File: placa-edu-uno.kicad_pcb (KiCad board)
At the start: 2 copper layers, 97.1 x 58.9 mm, 71 parts, among them J1 Conn_02x20_Odd_Even_MountingP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, J10 HEADER, J11 HEADER, J12 HEADER, J13 HEADER, J14 HEADER, J15 HEADER, J2 Screw_Terminal_01x02, J3 Screw_Terminal_01x02, J4 Screw_Terminal_01x02, J5 Screw_Terminal_01x02, J6 Conn_02x13_Odd_Even, J7 HEADER, J8 HEADER, J9 HEADER, U1 PCA9685, U2 MAX98357AETE_T, U3 MAX98357AETE_T, U4 ICS-43434, U5 ICS-43434, U6 LM73605

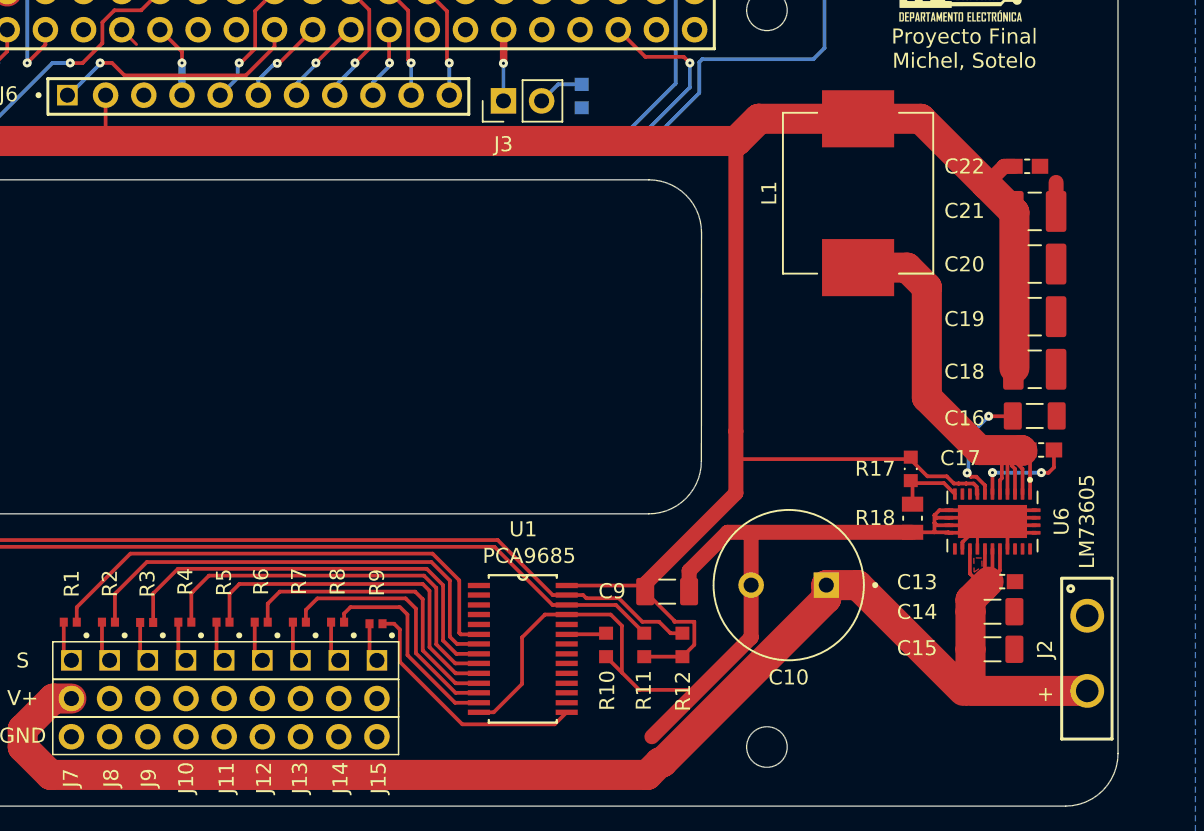
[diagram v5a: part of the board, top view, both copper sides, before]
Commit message: Se arranca un nuevo diseno. Se saco el regulador y 4 servos. Hay que reajustar el diseno del PCB.
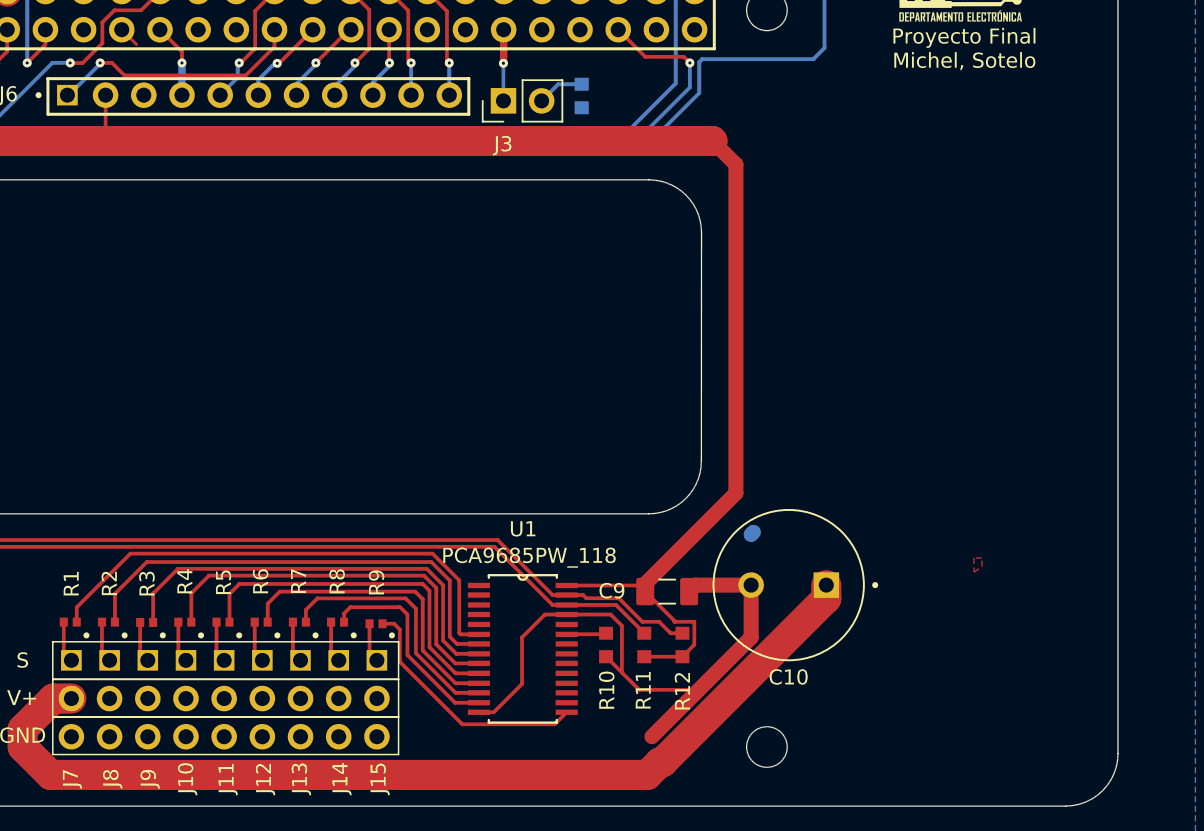
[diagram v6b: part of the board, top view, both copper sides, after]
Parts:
- removed C13, C22: 0.47 uF, CC0603KRX7R7BB474:CAPC1608X90
- removed C14, C15: 10 uF, CL31B106KOHNNNE:CAPC3216X180N
- removed C16: 2.2uF, CL31B225KOHNNNE:CAPC3216X180N
- removed C17: 0.47uF, CC0603KRX7R7BB474:CAPC1608X90
- removed C18, C19, C20, C21: 22uF, CL32B226KOJNNNE:CAPC3225X270N
- removed J2: Screw_Terminal_01x02, 691253700002:691253700002
- removed L1: 4.7uH, SPM10040T-4R7M:IND_SPM10040T-4R7M
- removed R17: 100k, 0603WAJ0104T5E:RESC1608X55N
- removed R18: 24.3k, 0805W8F2432T5E:RESC2012X65N
- removed U6: LM73605, LM73606RNPT-copia:QFN50P600X400X80-31N
- U1: value PCA9685 -> PCA9685PW_118
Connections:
- U1 pad 10: /Driver Servos/J4 -> unconnected-(U1-LED4-Pad10)
- U1 pad 11: /Driver Servos/J5 -> unconnected-(U1-LED5-Pad11)
- U1 pad 12: /Driver Servos/J6 -> unconnected-(U1-LED6-Pad12)
- U1 pad 13: /Driver Servos/J7 -> unconnected-(U1-LED7-Pad13)
- U1 pad 15: /Driver Servos/J8 -> unconnected-(U1-LED8-Pad15)
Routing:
- net 5V_RPI: track 190.1 -> 135.1 mm
- net GND: track 143.8 -> 89.8 mm
- net 5V_Fuente: track 103.1 -> 65.2 mm
- net Net-(C17-Pad1): track 34.3 -> 0.00 mm
- net Net-(U6-VCC): track 8.12 -> 0.00 mm, vias 2 -> 0
- net Net-(U6-CBOOT): track 7.07 -> 0.00 mm, vias 2 -> 0
- net Net-(U6-FB): track 4.69 -> 0.00 mm
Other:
- board text added: "FRENTE"

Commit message: Se borro todo y se arranco de nuevo. Placa circular.
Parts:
- removed J11, J12, J13, J14, J15: HEADER, TSW-101-07-T-T:SAMTEC_TSW-101-07-T-T
- removed the MountingHole at (3.50, 3.50)
- removed the MountingHole at (3.50, 52.5)
- removed R5, R6, R7, R8, R9: 220, RC0402FR-07220RL:RESC1005X40N
- U1: value PCA9685PW_118 -> PCA9685
- U2, U3: value MAX98357AETE_T -> MAX98357A
- moved C8 88.8 mm to (80.7, 35.1), turned to 90 degrees
- moved C4 88.3 mm to (80.7, 14.1), turned to -90 degrees
- moved FL3 87.1 mm to (79.2, 35.1), turned to -90 degrees
- moved FL1 86.7 mm to (79.2, 14.1), turned to -90 degrees
- moved FL4 85.4 mm to (77.7, 35.1), turned to -90 degrees
- moved FL2 85.1 mm to (77.7, 14.1), turned to -90 degrees
- moved C7 83.8 mm to (76.2, 35.1), turned to 90 degrees
- moved R13 83.6 mm to (82.3, 10.0)
- moved J5 83.6 mm to (73.6, 40.9), turned to 90 degrees
- moved J4 83.6 mm to (73.6, 19.8), turned to 90 degrees
- moved R14 83.4 mm to (82.3, 31.1)
- moved C3 83.4 mm to (76.2, 14.1), turned to 90 degrees
- moved U3 83.3 mm to (78.9, 30.8), turned to -90 degrees
- moved U2 82.7 mm to (78.9, 9.78), turned to -90 degrees
- moved C2 81.9 mm to (82.7, 12.7), turned to -90 degrees
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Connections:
- C10 pad 1: 5V_Fuente -> 5V_RPI
- J10 pad 02: 5V_Fuente -> 5V_RPI
- J7 pad 02: 5V_Fuente -> 5V_RPI
- J8 pad 02: 5V_Fuente -> 5V_RPI
- J9 pad 02: 5V_Fuente -> 5V_RPI
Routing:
- net 3.3V_RPI: track 130.1 -> 257.8 mm, vias 7 -> 5
- net 5V_Fuente: track 65.2 -> 0.00 mm
- net GPIO_21_DOUT_PCM: track 126.1 -> 61.5 mm, vias 1 -> 3
- net GPIO_20_DIN_PCM: track 115.5 -> 64.2 mm
- net GPIO_3_SCL_I2C: track 119.4 -> 77.5 mm
- net GPIO_18_CLK_PCM: track 94.3 -> 134.5 mm, vias 5 -> 4
- net GPIO_2_SDA_I2C: track 116.3 -> 77.7 mm
- net GND: track 89.8 -> 54.6 mm, vias 5 -> 8
- net 5V_RPI: track 135.1 -> 159.9 mm, vias 0 -> 1
- net /Driver Servos/J4: track 23.4 -> 0.00 mm
- net /Driver Servos/J5: track 20.1 -> 0.00 mm
- net /Driver Servos/J6: track 17.0 -> 0.00 mm
- net /Driver Servos/J8: track 16.6 -> 0.00 mm
- net /Driver Servos/J7: track 13.9 -> 0.00 mm
- net /Driver Servos/J0: track 33.5 -> 20.3 mm
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- added copper zone on F.Cu, net 5V_RPI
- removed copper zone on F.Cu, net 5V_Fuente
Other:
- board size 97.1 x 58.9 mm -> 96 x 96 mm
